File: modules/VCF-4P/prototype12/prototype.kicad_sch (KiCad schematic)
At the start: 38 parts, among them J1 Conn_01x09, U1 TL074, U2 SSI2140

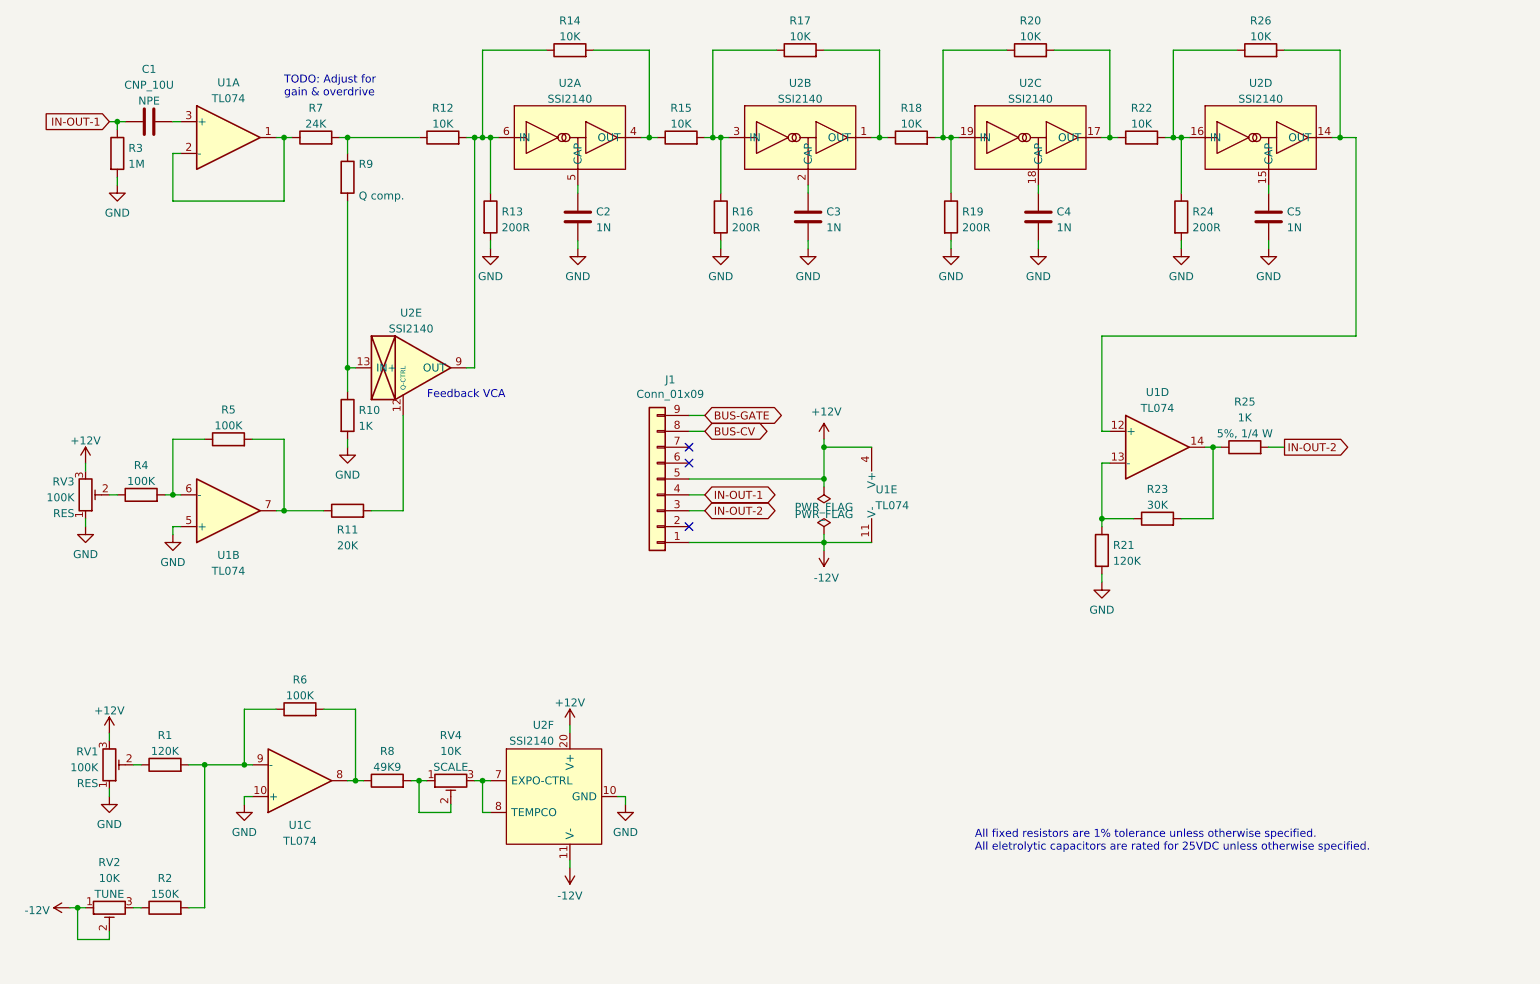
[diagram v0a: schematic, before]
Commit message: VCF-4P: Breadboard prototype, 2-pole version - wip
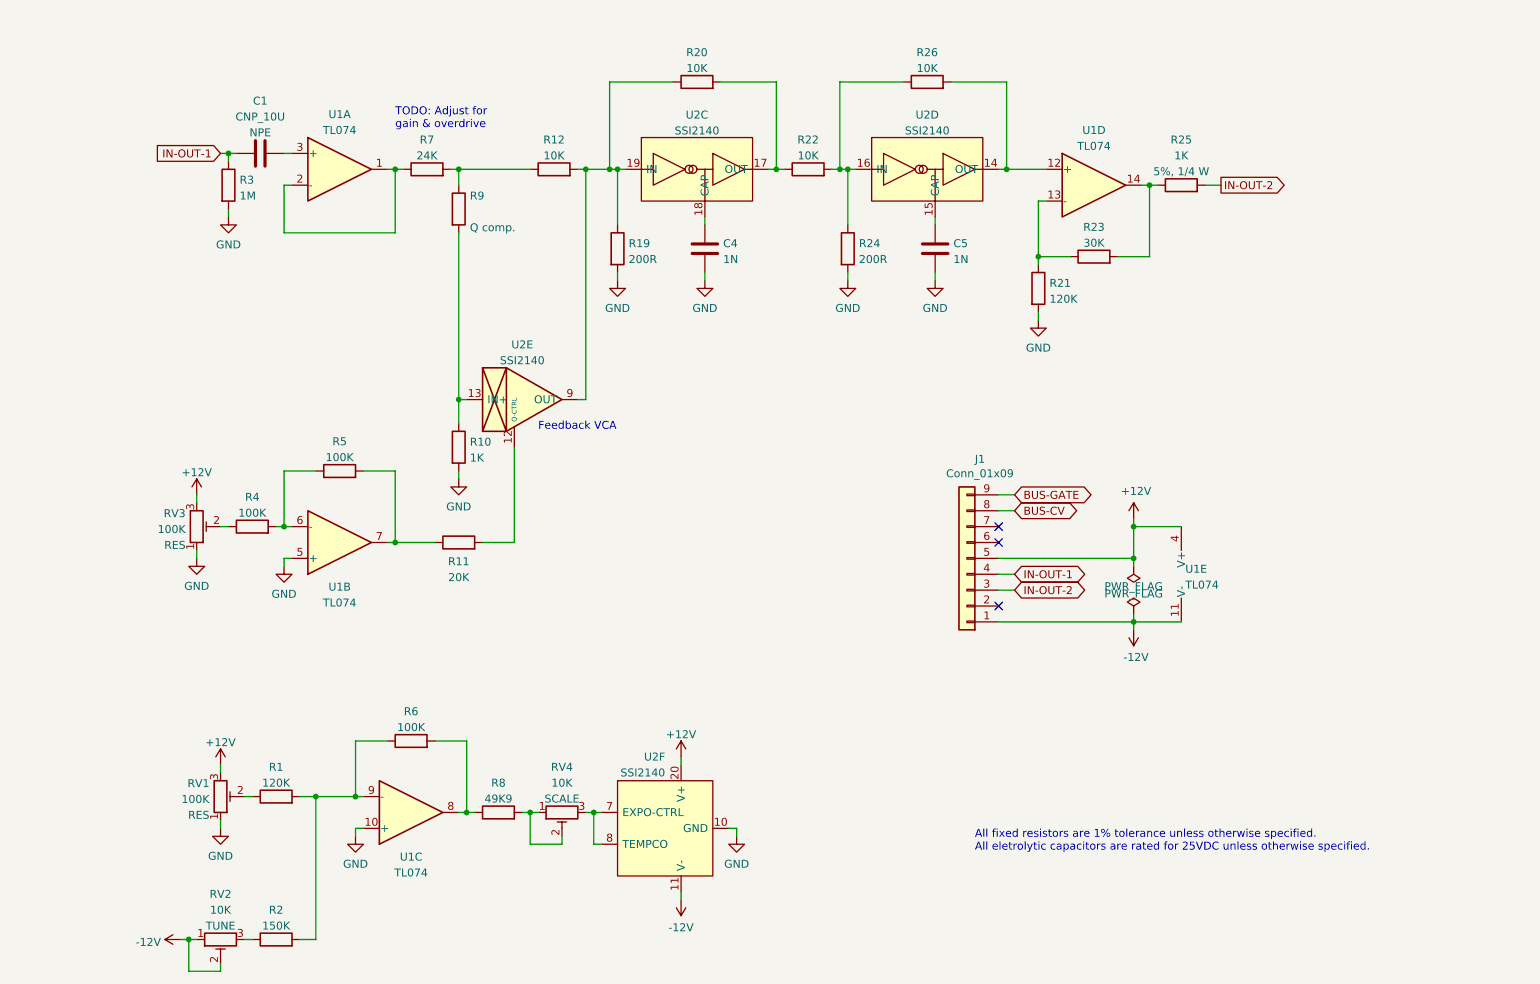
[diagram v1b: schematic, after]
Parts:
- removed C2, C3: 1N, -lmp-misc:C_Rect_Kemet_L7.2mm_W2.5mm_P5mm, symbol -lmp:CF
- removed R13, R16: 200R, -lmp-misc:R_Axial_DIN0207_L6.3mm_D2.5mm_P7.62mm_Horizontal, symbol -lmp:R_1%_0W166
- removed R14, R15, R17, R18: 10K, -lmp-misc:R_Axial_DIN0207_L6.3mm_D2.5mm_P7.62mm_Horizontal, symbol -lmp:R_1%_0W166
- removed unit 2 of U2
- removed unit 1 of U2
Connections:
- net at R19.1, R20.1, U2.19 (IN): now also R12.2, U2.9 (OUT)
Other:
- title: VCF-4P Prototype -> VCF Prototype - 2 Pole
- moved on the sheet: C1, C4, C5, J1, R1, R10, R11, R12, R19, R2, R20, R21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

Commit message: VCF-4P: Breadboard prototype, 2-pole version - wip
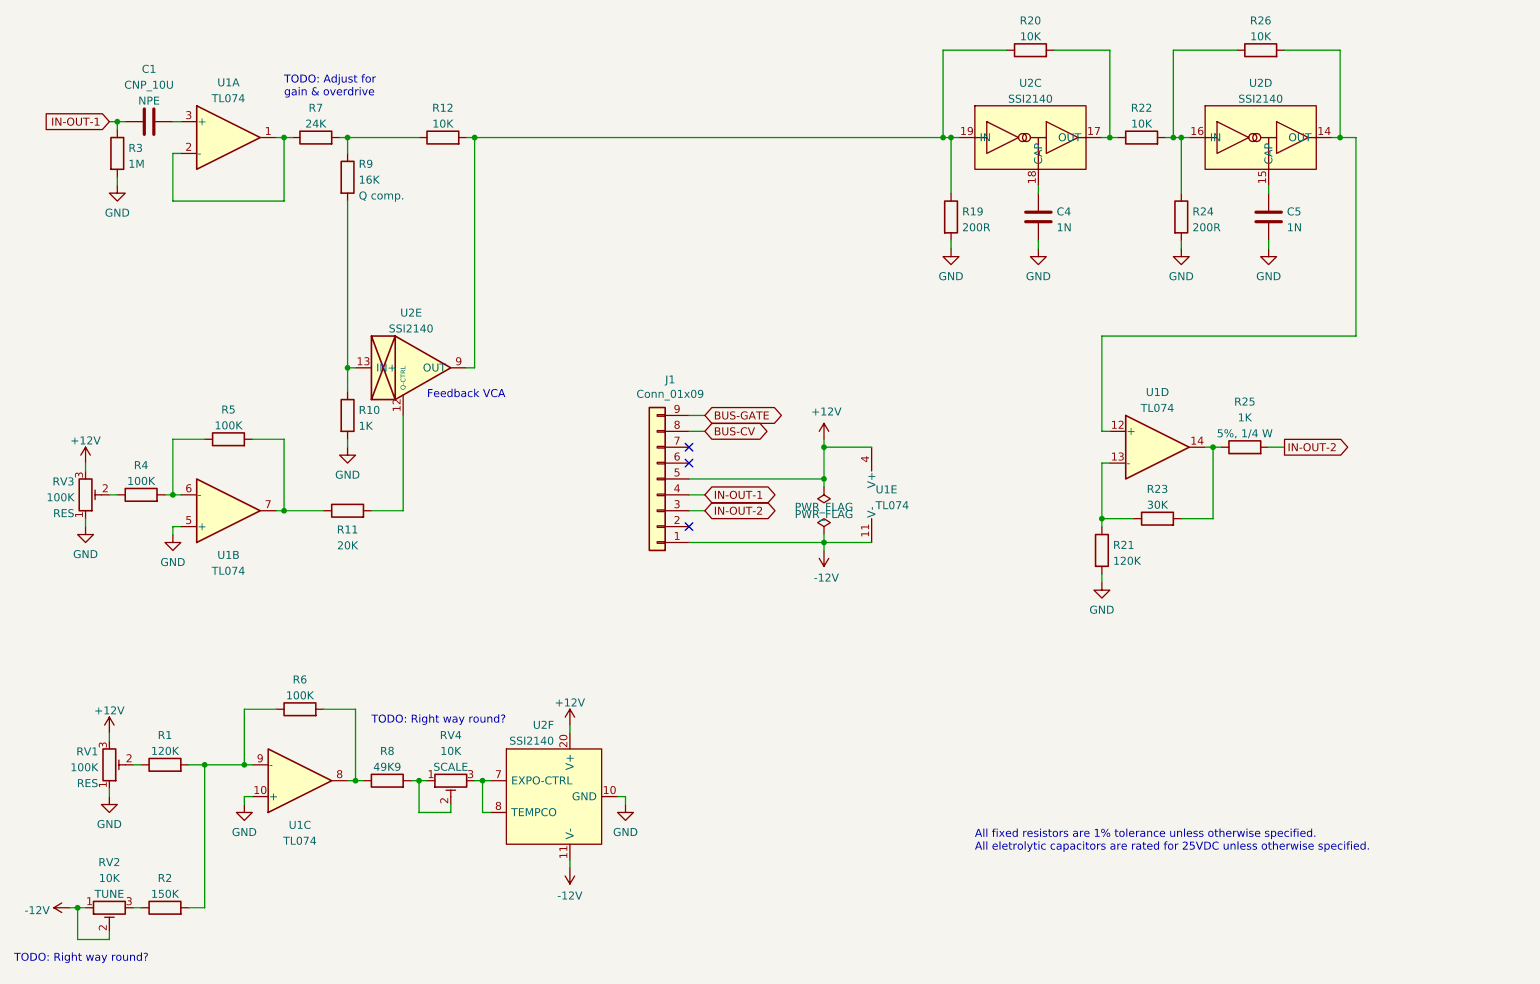
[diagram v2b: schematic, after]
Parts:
- R20, R26: footprint -lmp-misc:R_Axial_DIN0207_L6.3mm_D2.5mm_P7.62mm_Horizontal -> -lmp-stripboard:SB_Gen_2
- R22, R23, R5, R6: footprint -lmp-misc:R_Axial_DIN0207_L6.3mm_D2.5mm_P7.62mm_Horizontal -> -lmp-stripboard:SB_Gen_1
- R25: footprint -lmp-misc:R_Axial_DIN0207_L6.3mm_D2.5mm_P10.16mm_Horizontal -> -lmp-stripboard:SB_Gen_2
- R4: footprint -lmp-misc:R_Axial_DIN0207_L6.3mm_D2.5mm_P7.62mm_Horizontal -> -lmp-stripboard:SB_Gen_4
- R9: value (none) -> 16K; footprint (none) -> -lmp-misc:R_Axial_DIN0207_L6.3mm_D2.5mm_P7.62mm_Horizontal
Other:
- note added: "TODO: Right way round?"
- title: VCF Prototype - 2 Pole -> VCF 2-Pole Prototype
- moved on the sheet: C1, C4, C5, J1, R1, R10, R11, R12, R19, R2, R20, R21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
